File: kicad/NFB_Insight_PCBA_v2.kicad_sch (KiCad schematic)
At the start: 0 parts

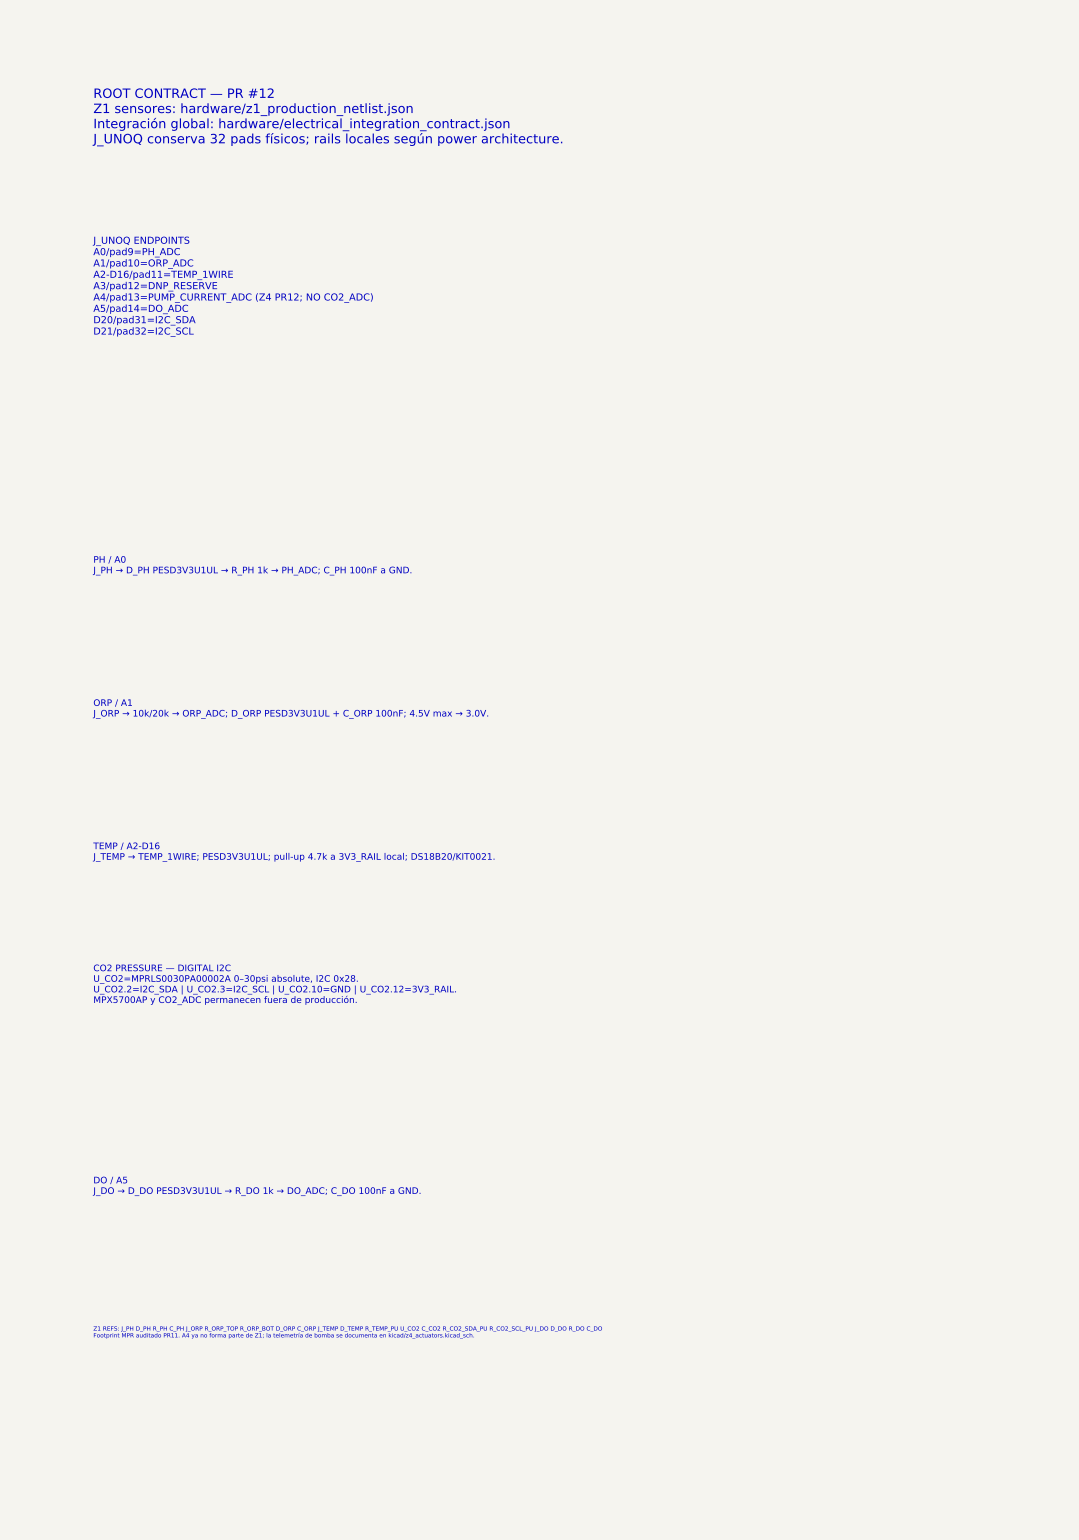
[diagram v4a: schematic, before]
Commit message: eda: integrar jerarquía raíz Z0-Z4 de Insight (#14)
Materializa la jerarquía inter-zona Z0-Z4 sin placement/routing. Congela una deuda ERC transitoria y reproducible de 125 label_dangling causada exclusivamente por la ausencia deliberada de símbolos internos, sin relajar severidades; cualquier otra violación falla CI. PR15 queda obligado a materializar símbolos/conectividad desde JSON/BOM y alcanzar ERC=0 antes de placement.
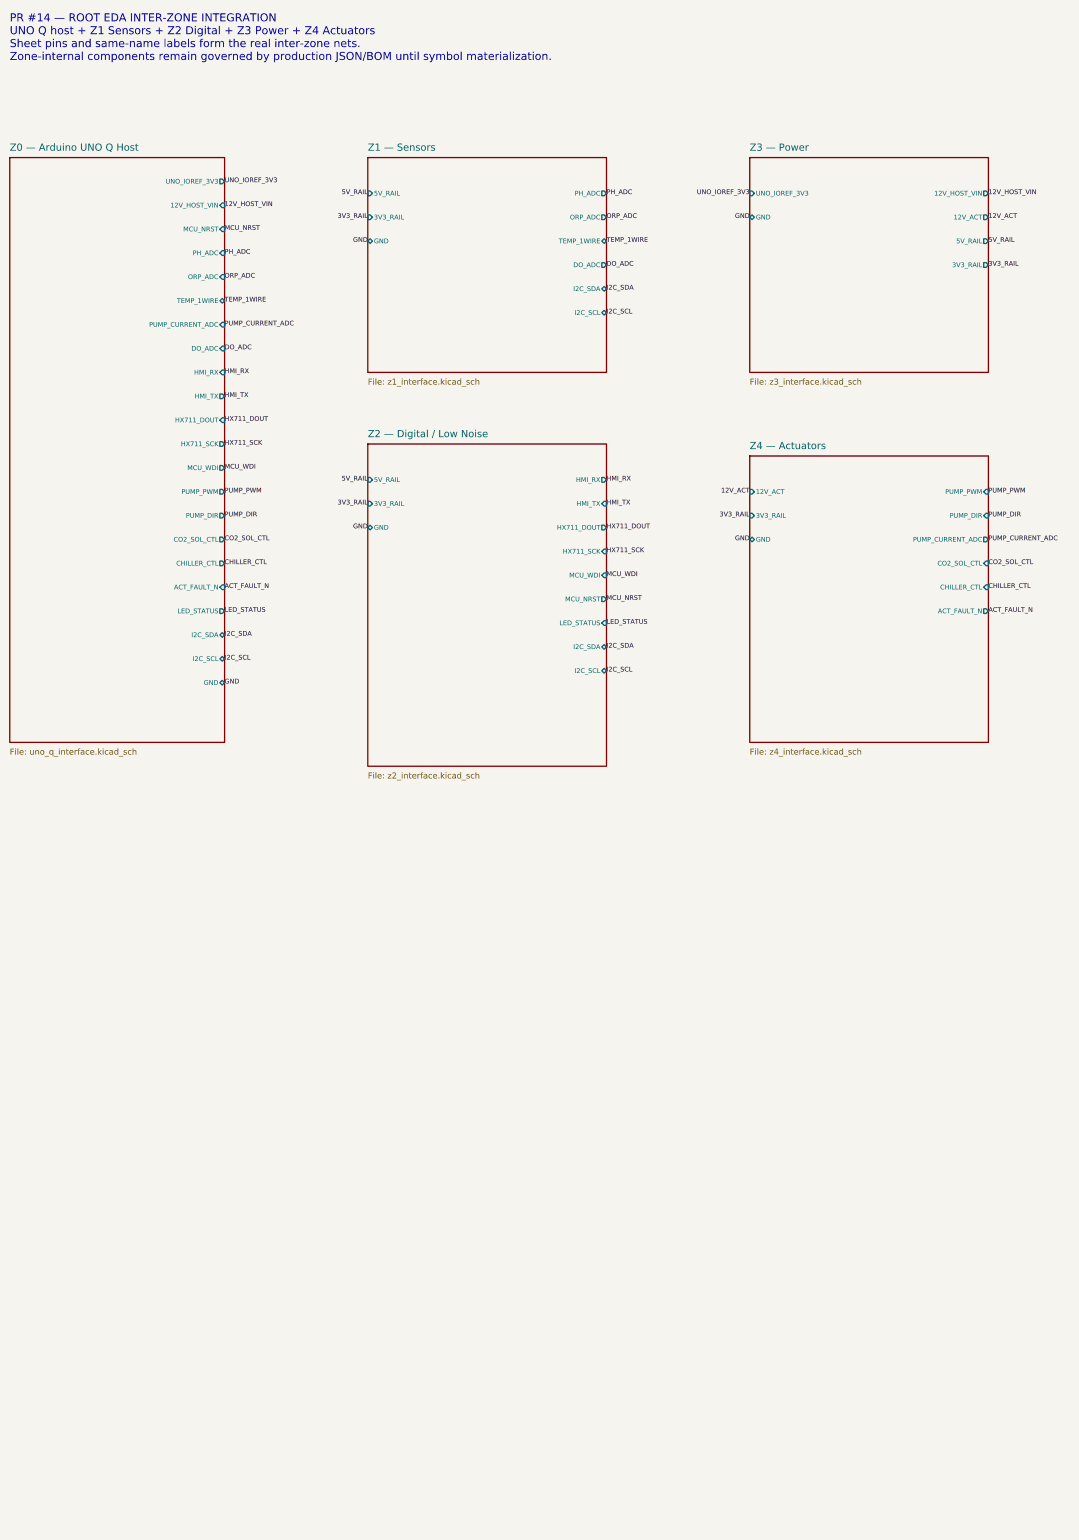
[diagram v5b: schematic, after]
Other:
- added sheet Z0 — Arduino UNO Q Host (uno_q_interface.kicad_sch)
- added sheet Z1 — Sensors (z1_interface.kicad_sch)
- added sheet Z2 — Digital / Low Noise (z2_interface.kicad_sch)
- added sheet Z3 — Power (z3_interface.kicad_sch)
- added sheet Z4 — Actuators (z4_interface.kicad_sch)
- note added: "PR #14 — ROOT EDA INTER-ZONE INTEGRATION UNO Q host + Z1 Sensors + Z2 Digital + Z3 Power + Z4 Actuators Sheet pins and same-name labels form the real inter-zone nets. Zone-internal components remain governed by production JSON/BOM until symbol materialization."
- note removed: "CO2 PRESSURE — DIGITAL I2C U_CO2=MPRLS0030PA00002A 0–30psi absolute, I2C 0x28. U_CO2.2=I2C_SDA | U_CO2.3=I2C_SCL | U_CO2.10=GND | U_CO2.12=3V3_RAIL. MPX5700AP y CO2_ADC permanecen fuera de producción."
- note removed: "DO / A5 J_DO → D_DO PESD3V3U1UL → R_DO 1k → DO_ADC; C_DO 100nF a GND."
- note removed: "J_UNOQ ENDPOINTS A0/pad9=PH_ADC A1/pad10=ORP_ADC A2-D16/pad11=TEMP_1WIRE A3/pad12=DNP_RESERVE A4/pad13=PUMP_CURRENT_ADC (Z4 PR12; NO CO2_ADC) A5/pad14=DO_ADC D20/pad31=I2C_SDA D21/pad32=I2C_SCL"
- note removed: "ORP / A1 J_ORP → 10k/20k → ORP_ADC; D_ORP PESD3V3U1UL + C_ORP 100nF; 4.5V max → 3.0V."
- note removed: "PH / A0 J_PH → D_PH PESD3V3U1UL → R_PH 1k → PH_ADC; C_PH 100nF a GND."
- note removed: "ROOT CONTRACT — PR #12 Z1 sensores: hardware/z1_production_netlist.json Integración global: hardware/electrical_integration_contract.json J_UNOQ conserva 32 pads físicos; rails locales según power architecture."
- note removed: "TEMP / A2-D16 J_TEMP → TEMP_1WIRE; PESD3V3U1UL; pull-up 4.7k a 3V3_RAIL local; DS18B20/KIT0021."
- note removed: "Z1 REFS: J_PH D_PH R_PH C_PH J_ORP R_ORP_TOP R_ORP_BOT D_ORP C_ORP J_TEMP D_TEMP R_TEMP_PU U_CO2 C_CO2 R_CO2_SDA_PU R_CO2_SCL_PU J_DO D_DO R_DO C_DO Footprint MPR auditado PR11. A4 ya no forma parte de Z1; la telemetría de bomba se documenta en kicad/z4_actuators.kicad_sch."
- title: NFB Insight PCBA v2 — Root Contract / Z1 Sensors -> NFB Insight PCBA v2 — Root EDA Inter-Zone Hierarchy
